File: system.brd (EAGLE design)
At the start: 41.8 x 68.2 mm, 122 parts, among them IC1 TPS7B8650BQDDARQ1, J1 TSW-104-07-F-S, J2 163-179PH-EX, J3 RS1-02-G, SW1 1825910-6, SW2 1825910-6, SW3 1825910-6, U1 ATMEGA328PB-AU, Y1 ABL-16.000MHZ-B2

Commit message: created 3d model for all libraries. routing
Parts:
- removed ADC:IC3: TLV9021QDBVRQ1, TLV9021QDBVRQ1:SOT95P280X145-5N
- removed BUCK:SW, TP19, TP_1V5, TP_2V5, TP_5V, TP_6V: TPPAD1-13, testpad:P1-13
- removed SV1: programming pins, con-lstb:MA04-1
- added ADC:IC2: TLV9021QDBVRQ1, TLV9021QDBVRQ1:SOT95P280X145-5N
- added BK:TP1, TP1, TP15, TP2, TP3, TP4: 5010, 5010:5010
- added J4: TSW-104-07-F-S, TSW-104-07-F-S:SAMTEC_TSW-104-07-F-S
- J1: value TSW-104-07-F-S -> OLED
- R5, R6: value 10000 -> 10k
- TP10, TP11, TP12, TP13, TP14, TP16, TP17, TP5, TP6, TP7, TP8, TP9: value TPPAD1-13 -> 5010; device testpad:P1-13 -> 5010:5010
- TT:C1, TT:C2, TT:C3: device BeagleBone_Black_Wireless:C0603 -> resistor:C0603
- moved TP10 167.8 mm to (-75.1, -0.38)
- moved TP13 164.7 mm to (-75.1, -16.4)
- moved TP5 161.1 mm to (-75.1, 26.3)
- moved TP14 160.1 mm to (-75.1, -21.7)
- moved TP16 157.5 mm to (-75.1, -32.4)
- moved TP7 154.0 mm to (-75.1, 15.6)
- moved TP17 153.7 mm to (-75.1, -37.7)
- moved TP8 150.9 mm to (-75.1, 10.3)
- moved TP9 148.1 mm to (-75.1, 4.95)
- moved TT:C2 144.7 mm to (-80.0, -59.4)
- moved TT:C3 133.7 mm to (-80.0, -63.2), flipped to the top, turned to 0 degrees
- moved TP11 131.3 mm to (-75.1, -5.71)
- moved Y1 115.0 mm to (-75.4, -49.5), flipped to the top, turned to 0 degrees
- moved TP6 106.9 mm to (-75.1, 21.0)
- moved TT:C1 103.2 mm to (-60.6, 63.2), flipped to the top, turned to 0 degrees
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- renumbered BUCK:C1 to BK:C1, BUCK:C2 to BK:C2, BUCK:C2_2 to BK:C2_2, BUCK:C3 to BK:C3, BUCK:C5 to BK:C5, BUCK:C6 to BK:C6, BUCK:IC1 to BK:IC1, BUCK:L1 to BK:L1, BUCK:R1 to BK:R1, BUCK:R2 to BK:R2, BUCK:R5 to BK:R5, BUCK:RT to BK:RT, BUCK:S1 to BK:S1
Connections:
- net BUCK:EN renamed BK:EN
- net BUCK:N$1 renamed BK:N$1
- net BUCK:N$3 renamed BK:N$3
- net BUCK:N$4 renamed BK:N$4
- net BUCK:N$5 renamed BK:N$5
- net BUCK:N$6 renamed BK:N$6
- net BUCK:N$7 renamed BK:N$7
- removed net BUCK:N$2: BK:C3.2, BK:IC1.8, BK:L1.1, BUCK:SW.TP
- new net BK:N$2: BK:C3.2, BK:IC1.8, BK:L1.1, BK:TP1.1
- net 0: now also ADC:IC2.2; no longer ADC:IC3.2
- net ADC:N$2: now also ADC:IC2.3; no longer ADC:IC3.3
- net ADC_EXT_INT: now also TP10.1; no longer TP11.TP
- net MCU_RST: now also J4.01, TP15.1; no longer SV1.1, TP17.TP
- net MISO_MCU: now also J4.03, TP12.1; no longer SV1.3, TP13.TP
- net MOSI_MCU: now also J4.02, TP13.1; no longer SV1.2, TP14.TP
- net N$14: now also ADC:IC2.1; no longer ADC:IC3.1
- net N$4: now also TP17.1; no longer TP12.TP
- net N$5: now also ADC:IC2.4; no longer ADC:IC3.4
- net N$6: now also ADC:IC2.5; no longer ADC:IC3.5
- net PB_START: now also TP14.1; no longer TP16.TP
- net RST_ADC: now also TP9.1; no longer TP10.TP
- net SCK_MCU: now also J4.04; no longer SV1.4
- net SDA: now also TP16.1; no longer TP19.TP
- net VS_1.5V_OUT: now also TP4.1; no longer TP_1V5.TP
- net VS_2.5V_OUT: now also TP3.1; no longer TP_2V5.TP
- net VS_5V_OUT: now also TP2.1; no longer TP_5V.TP
- net VS_6V: now also TP1.1; no longer TP_6V.TP
- net V_BG: now also TP6.1; no longer TP6.TP
- net V_SIG: now also TP8.1; no longer TP9.TP
- net V_TH: now also TP5.1; no longer TP5.TP
- net V_TOGGLE: now also TP11.1; no longer TP8.TP
- net V_TP: now also TP7.1; no longer TP7.TP
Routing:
- net BUCK:N$2: track 21.3 -> 0.00 mm, vias 1 -> 0
- net BK:N$2: track 0.00 -> 16.5 mm, vias 0 -> 1
- net VS_2.5V_OUT: track 33.7 -> 27.6 mm
- net ADC:N$2: track 7.88 -> 4.37 mm
- net VS_5V_OUT: track 35.6 -> 32.3 mm
- net VS_6V: track 38.6 -> 36.9 mm
- net EXT_CLK_2: track 17.5 -> 15.9 mm
- net N$6: track 4.95 -> 4.10 mm

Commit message: routing
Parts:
- removed BK:TP1, TP1, TP11, TP12, TP13, TP14, TP15, TP16, TP17, TP2, TP3, TP4, TP5, TP6, TP7, TP8, TP9: 5010, 5010:5010
- added 1.5V, 2.5V, 5V, 6V, AVCC, BK:SW_NODE, MCU_RST, MISO_MCU, MOSI_MCU, PB_START, RST_ADC, SDA, V_BG, V_SIG, V_TH, V_TOGGLE, V_TP: 5010, 5010:5010
- J3: value RS1-02-G -> AD2
- J4: value TSW-104-07-F-S -> MCU
- moved Y1 114.8 mm to (11.0, 25.9), flipped to the bottom, turned to 180 degrees
- moved TT:C2 111.1 mm to (-15.2, 30.9)
- moved TT:C3 109.6 mm to (-15.2, 25.1), turned to 90 degrees
- moved TP10 89.0 mm to (11.8, 19.1)
- moved R19 87.0 mm to (24.8, -4.32), turned to 90 degrees
- moved J4 86.5 mm to (2.67, 11.8), turned to 90 degrees
- moved R17 84.9 mm to (35.9, -2.29)
- moved R18 77.2 mm to (28.6, 12.2)
- moved C6 66.8 mm to (16.9, 3.05), flipped to the bottom
- moved TT:C1 57.3 mm to (-15.2, 28.2)
- moved R5 54.8 mm to (8.76, 16.3), flipped to the bottom
- moved J3 35.0 mm to (36.2, 28.4), turned to 0 degrees
- moved L1 23.4 mm to (31.8, 8.64), flipped to the bottom
- moved R23 5.29 mm to (40.0, 32.4), turned to 270 degrees
- moved C9 4.95 mm to (17.4, 16.9)
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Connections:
- net BK:N$2: now also BK:SW_NODE.1; no longer BK:TP1.1
- net MCU_RST: now also MCU_RST.1; no longer TP15.1
- net MISO_MCU: now also MISO_MCU.1; no longer TP12.1
- net MOSI_MCU: now also MOSI_MCU.1; no longer TP13.1
- net N$4: now also AVCC.1; no longer TP17.1
- net PB_START: now also PB_START.1; no longer TP14.1
- net RST_ADC: now also RST_ADC.1; no longer TP9.1
- net SDA: now also SDA.1; no longer TP16.1
- net VS_1.5V_OUT: now also 1.5V.1; no longer TP4.1
- net VS_2.5V_OUT: now also 2.5V.1; no longer TP3.1
- net VS_5V_OUT: now also 5V.1; no longer TP2.1
- net VS_6V: now also 6V.1; no longer TP1.1
- net V_BG: now also V_BG.1; no longer TP6.1
- net V_SIG: now also V_SIG.1; no longer TP8.1
- net V_TH: now also V_TH.1; no longer TP5.1
- net V_TOGGLE: now also V_TOGGLE.1; no longer TP11.1
- net V_TP: now also V_TP.1; no longer TP7.1
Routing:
- net EXT_CLK_1: track 11.7 -> 7.06 mm
- net VS_6V: track 36.9 -> 39.4 mm
- net EXT_CLK_2: track 15.9 -> 16.8 mm
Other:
- board size 41.8 x 68.2 mm -> 49.4 x 68.2 mm

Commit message: pcb
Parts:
- moved AVCC 32.5 mm to (-17.9, 4.19)
- moved BK:SW_NODE 26.7 mm to (33.5, 64.8)
- moved SDA 25.5 mm to (-17.1, -3.81)
- moved RST_ADC 23.5 mm to (-7.62, -5.33)
- moved V_TOGGLE 23.2 mm to (3.81, -9.91)
- moved TP10 18.9 mm to (-4.95, 27.8)
- moved V_TH 18.8 mm to (-11.0, 11.4)
- moved R18 11.8 mm to (23.6, 1.52)
- moved C8 11.4 mm to (14.1, 17.9), flipped to the top, turned to 180 degrees
- moved C11 11.1 mm to (14.1, 20.3), turned to 180 degrees
- moved ADC:IC1 9.76 mm to (19.4, -1.91)
- moved R23 7.97 mm to (37.0, 25.0), turned to 0 degrees
- moved 6V 6.48 mm to (40.0, 65.2)
- moved L1 5.31 mm to (33.7, 3.68)
- moved J1 4.64 mm to (2.41, 1.52), turned to 90 degrees
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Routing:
- net V_BG: track 11.8 -> 29.5 mm, vias 1 -> 2
- net EXT_CLK_2: track 16.8 -> 0.00 mm
- net EXT_CLK_1: track 7.06 -> 0.08 mm
- net BK:N$2: track 16.5 -> 22.0 mm
- net VS_1.5V_OUT: track 10.5 -> 7.51 mm
- net N$11: track 0.00 -> 2.81 mm
- net VS_5V_OUT: track 32.3 -> 30.2 mm
- net VS_6V: track 39.4 -> 40.3 mm
- net N$19: track 30.1 -> 30.6 mm
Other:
- board size 49.4 x 68.2 mm -> 49.4 x 74 mm

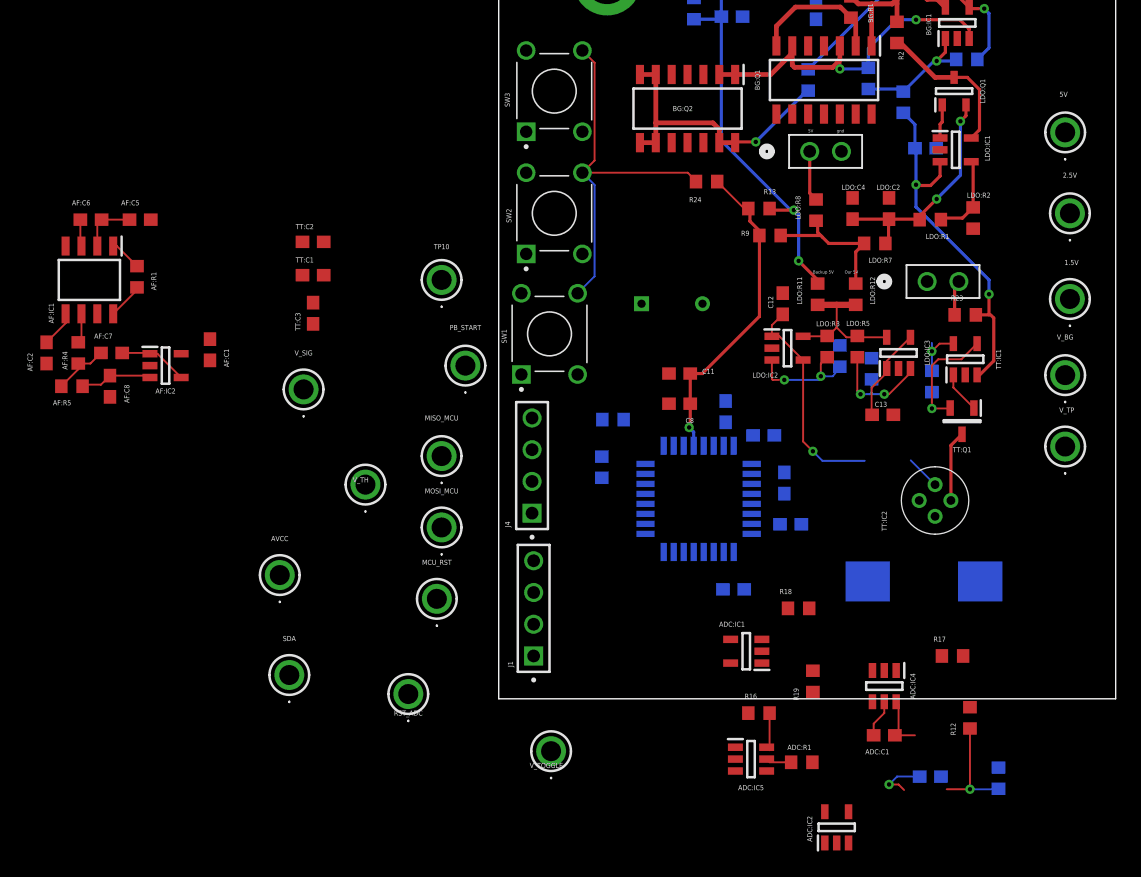
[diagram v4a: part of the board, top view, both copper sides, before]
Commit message: Placed AF module on backside of PCB
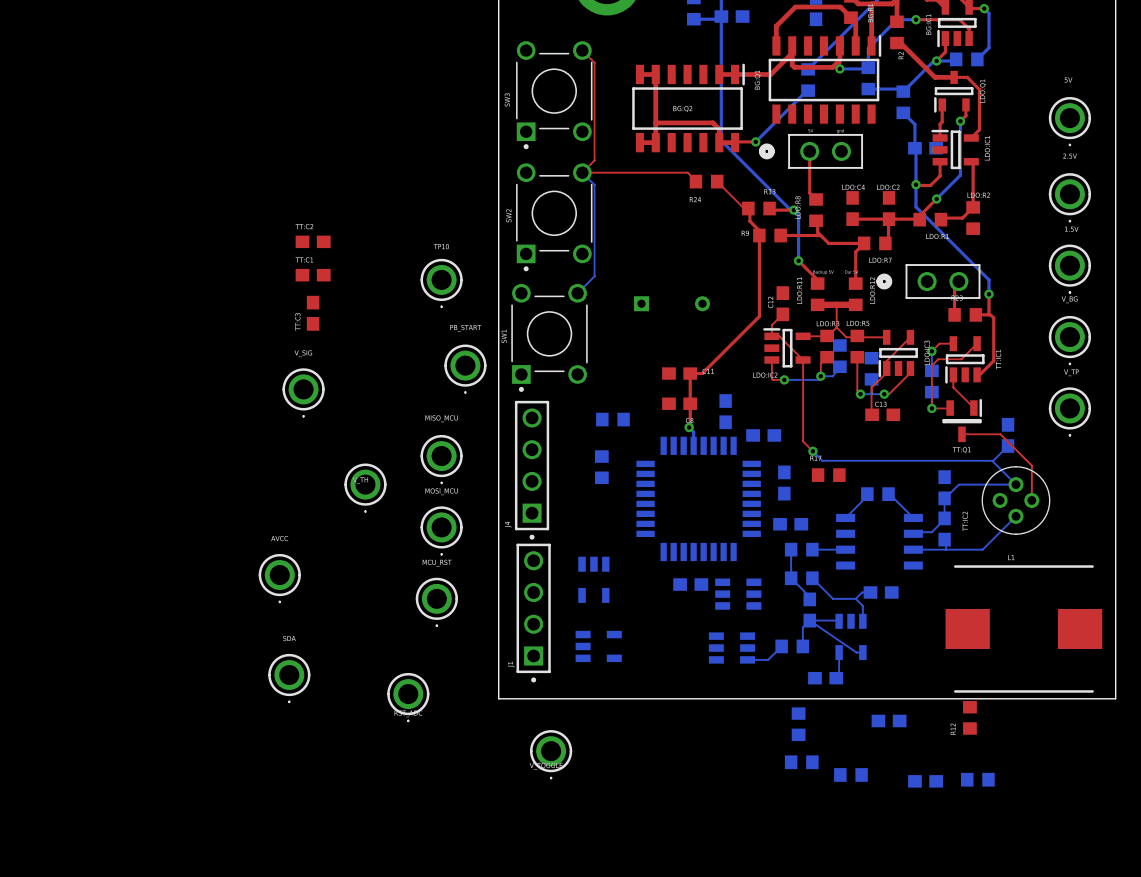
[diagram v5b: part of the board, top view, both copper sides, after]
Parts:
- moved AF:C2 77.2 mm to (40.4, 15.4), flipped to the bottom, turned to 90 degrees
- moved AF:C6 72.7 mm to (35.3, 7.87), flipped to the bottom, turned to 90 degrees
- moved AF:C5 67.9 mm to (35.3, 11.2), flipped to the bottom, turned to 90 degrees
- moved AF:IC1 66.6 mm to (30.1, 6.86), flipped to the bottom, turned to 0 degrees
- moved AF:C8 63.9 mm to (30.2, 2.79), flipped to the bottom, turned to 180 degrees
- moved AF:R1 61.8 mm to (30.0, 10.7), flipped to the bottom, turned to 0 degrees
- moved AF:R5 60.4 mm to (23.9, 3.94), flipped to the bottom, turned to 180 degrees
- moved AF:R4 60.0 mm to (23.9, 6.22), flipped to the bottom, turned to 0 degrees
- moved AF:C7 59.5 mm to (24.5, 1.40), flipped to the bottom, turned to 270 degrees
- moved AF:IC2 59.0 mm to (27.8, -0.76), flipped to the bottom, turned to 270 degrees
- moved AF:C1 55.9 mm to (25.8, -4.06), flipped to the bottom, turned to 0 degrees
- moved ADC:IC2 27.8 mm to (7.24, 3.81), flipped to the bottom, turned to 270 degrees
- moved R17 17.5 mm to (26.0, 12.2)
- moved R18 14.0 mm to (27.8, -11.8), flipped to the bottom
- moved ADC:IC4 13.8 mm to (18.8, 2.67), flipped to the bottom, turned to 180 degrees
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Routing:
- net VS_2.5V_OUT: track 27.7 -> 43.0 mm
- net N$14: track 9.12 -> 0.00 mm, vias 1 -> 0
- net V_TP: track 2.56 -> 10.2 mm
- net ADC:N$2: track 4.37 -> 0.00 mm
- net V_SIG: track 5.53 -> 9.72 mm
- net N$6: track 4.10 -> 0.00 mm, vias 1 -> 0
- net V_TH: track 5.67 -> 9.42 mm
- net ADC:N$4: track 3.13 -> 0.00 mm
- net ADC:N$1: track 2.07 -> 0.00 mm
- net AF:N$7: track 5.81 -> 7.58 mm
- net VS_5V_OUT: track 30.2 -> 31.7 mm

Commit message: Update system.brd
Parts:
- moved ADC:C1 24.8 mm to (6.73, -1.91), turned to 270 degrees
- moved R18 15.6 mm to (14.5, -3.81), flipped to the top
- moved ADC:R1 13.5 mm to (14.4, -1.27)
- moved ADC:IC1 2.32 mm to (9.91, -1.14), turned to 90 degrees
- moved AF:C1 2.16 mm to (27.9, -3.94), turned to 180 degrees
- moved ADC:IC2 1.37 mm to (8.00, 4.95), turned to 90 degrees
- moved ADC:IC5 0.36 mm to (18.5, -1.91), turned to 270 degrees
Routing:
- net ADC:N$4: track 0.00 -> 9.18 mm
- net ADC:N$2: track 0.00 -> 7.53 mm
- net N$5: track 0.00 -> 6.90 mm, vias 0 -> 1
- net ADC:N$1: track 0.00 -> 4.71 mm
- net N$2: track 3.17 -> 7.74 mm

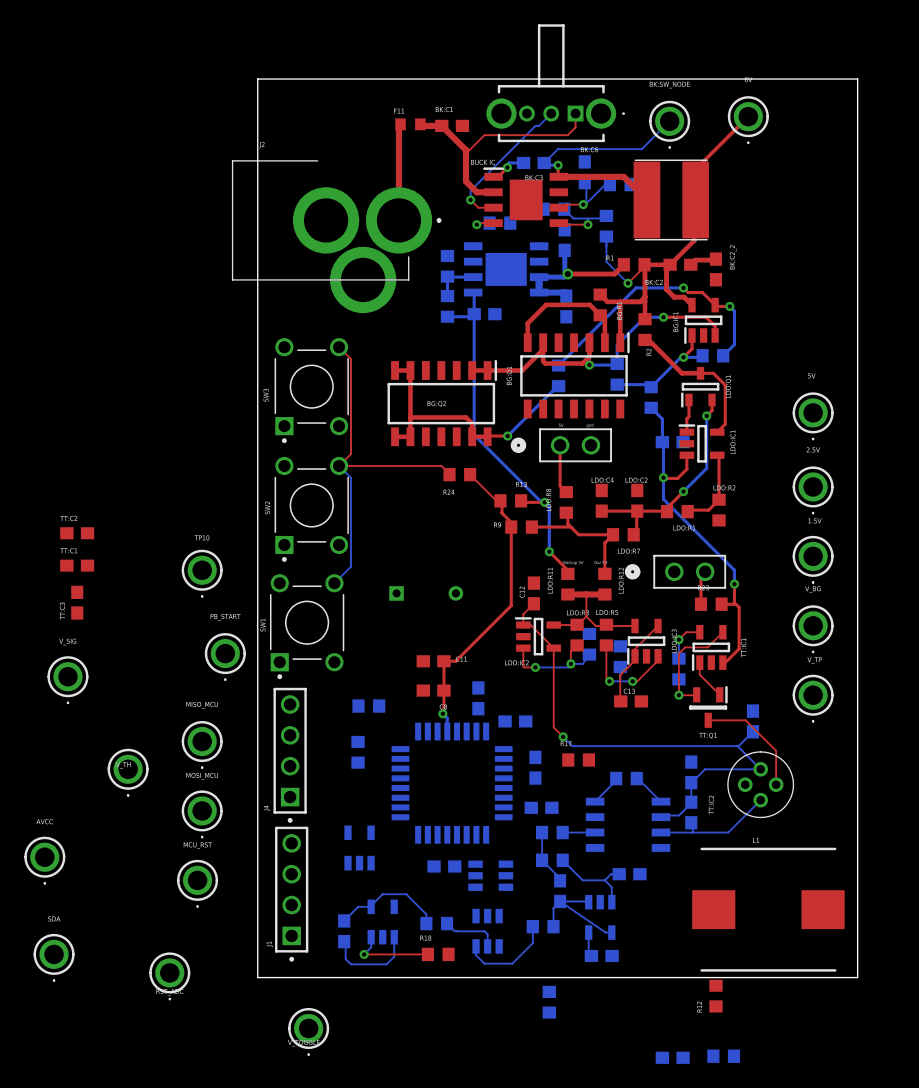
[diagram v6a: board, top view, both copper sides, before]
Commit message: made board bigger so sections wip
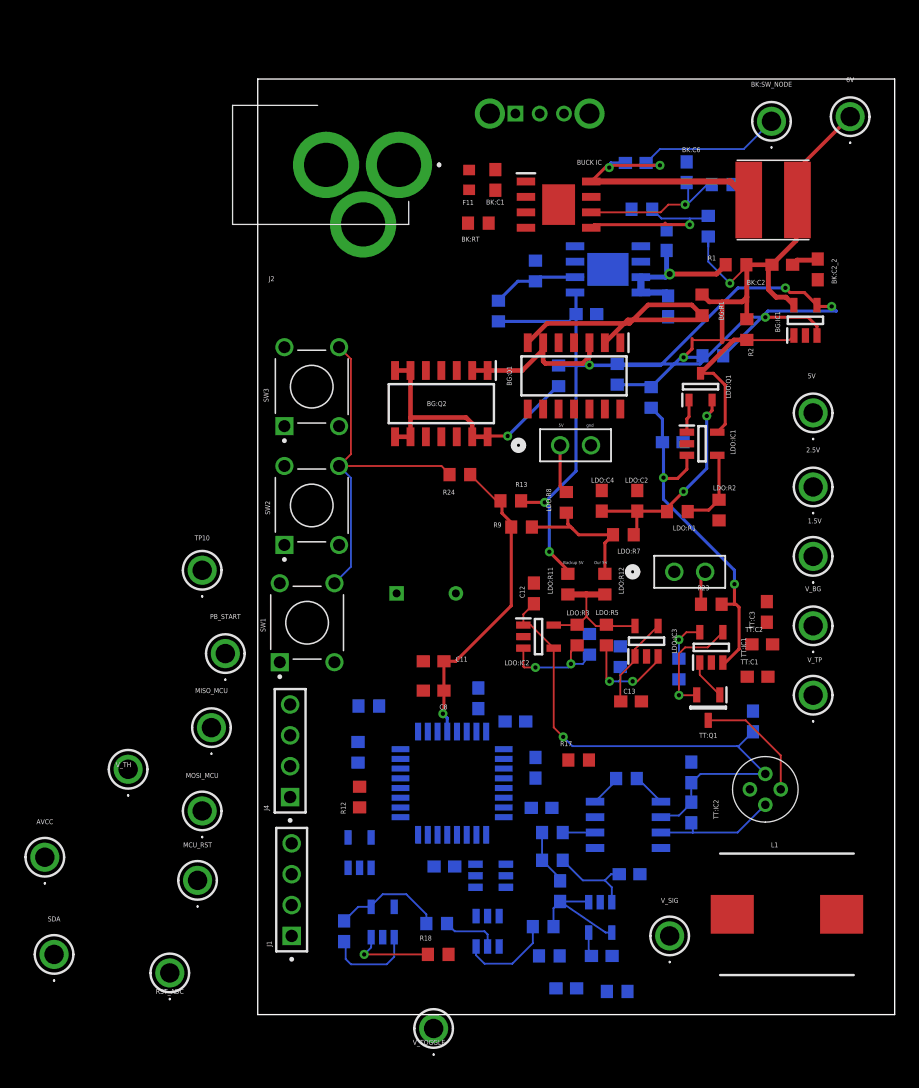
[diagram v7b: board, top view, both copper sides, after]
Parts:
- moved TT:C2 57.1 mm to (41.1, 21.7)
- moved TT:C3 56.8 mm to (41.5, 24.4)
- moved TT:C1 56.7 mm to (40.8, 19.1)
- moved V_SIG 53.9 mm to (33.5, -2.29)
- moved R12 33.6 mm to (8.00, 9.14)
- moved ADC:C2 10.5 mm to (25.0, -6.60)
- moved V_TOGGLE 10.3 mm to (14.1, -9.91)
- moved ADC:R2 10.3 mm to (29.2, -6.86)
- moved C3 8.38 mm to (33.4, 49.5)
- moved BG:R1 8.38 mm to (36.2, 49.7)
- moved BK:C3 8.38 mm to (30.7, 61.3)
- moved BK:R1 8.38 mm to (36.7, 56.1)
- moved C2 8.38 mm to (33.3, 55.0)
- moved C5 8.38 mm to (26.7, 48.9)
- moved IC1 8.38 mm to (28.4, 52.6)
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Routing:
- net VS_9V: track 21.6 -> 0.08 mm
- net BG:N$4: track 22.0 -> 37.1 mm
- net BG:N$1: track 11.0 -> 25.7 mm
- net BK:EN: track 12.2 -> 0.00 mm, vias 1 -> 0
- net BK:N$2: track 22.0 -> 32.8 mm
- net BK:N$6: track 6.85 -> 15.8 mm
- net N$7: track 10.6 -> 18.8 mm
- net N$3: track 8.08 -> 0.00 mm
- net BG:N$2: track 30.2 -> 37.6 mm
- net BK:N$5: track 6.97 -> 12.8 mm
- net N$10: track 4.37 -> 7.75 mm
- net VS_5V_BACKUP: track 30.3 -> 33.2 mm
- net BK:N$1: track 2.54 -> 0.00 mm, vias 1 -> 0
- net BK:N$3: track 3.06 -> 1.60 mm
- net VS_2.5V_OUT: track 43.0 -> 43.8 mm
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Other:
- board size 49.4 x 74 mm -> 52.4 x 77 mm
